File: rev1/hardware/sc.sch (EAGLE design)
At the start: 99 parts, among them IC1 PB137ACV, IC2 INA168, Q1 si2305cd, Q2 8MHz 18pF, Q3 IRFR5305, T1 BC846, U1 SPX5205 3v3, U6 microSD Socket, X3 MKDSN1,5/4-5,08, Y1 32768Hz CFPX-217 12.5pF

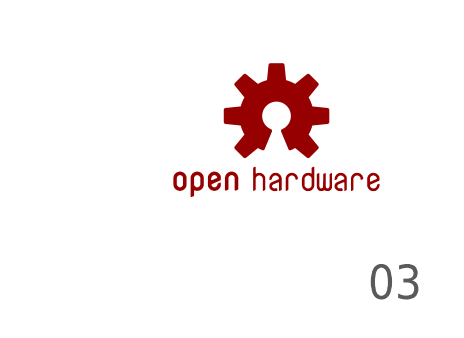
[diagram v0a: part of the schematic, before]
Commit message: rev2 routing 2/3
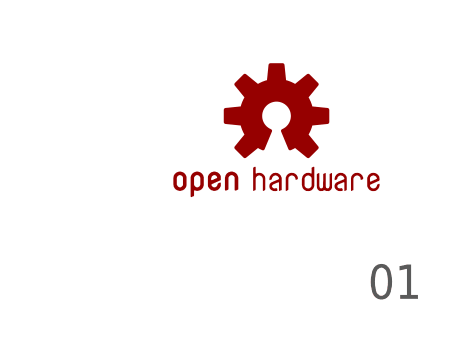
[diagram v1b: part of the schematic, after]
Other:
- note added: "01"
- note removed: "03"
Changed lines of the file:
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@@
 <?xml version="1.0" encoding="utf-8"?>
 <!DOCTYPE eagle SYSTEM "eagle.dtd">
-<eagle version="6.5.0">
+<eagle version="7.3.0">
 <drawing>
 <settings>
@@
 <sheet>
 <plain>
-<text x="416.56" y="10.16" size="3.81" layer="97">03</text>
+<text x="416.56" y="10.16" size="3.81" layer="97">01</text>
 <text x="264.16" y="177.8" size="1.778" layer="97">uC pins: 7 11 28</text>
 </plain>
